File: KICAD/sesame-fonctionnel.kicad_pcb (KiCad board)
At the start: 2 copper layers, 160 x 100 mm, 278 parts, among them J1 CXS70-14-C, J2 CXS70-14-C, J7 CXS70-14-C, J8 CXS70-14-C, J9 Conn_02x16_Odd_Even, Q1 BC847, Q10 BC857, Q11 SQM120, Q12 BC847, Q13 BC847, Q2 BC847, Q3 BC847, Q4 BC847, Q5 BC847, Q6 SQM120, Q7 BC857, Q8 SQM120, Q9 SQM120, U1 AD8030, U10 LT6016, U11 AD8030, U12 UCC27284-Q1, U13 AD8030, U14 AD8030, U15 LT8365, U16 LM4040DBZ-2.5, U17 UCC27284-Q1, U2 LM2903, U3 CD4053BM96, U4 4011, U5 CD4053BM96, U6 CD4053BM96, U7 AD8030, U8 LT6016, U9 AD8030

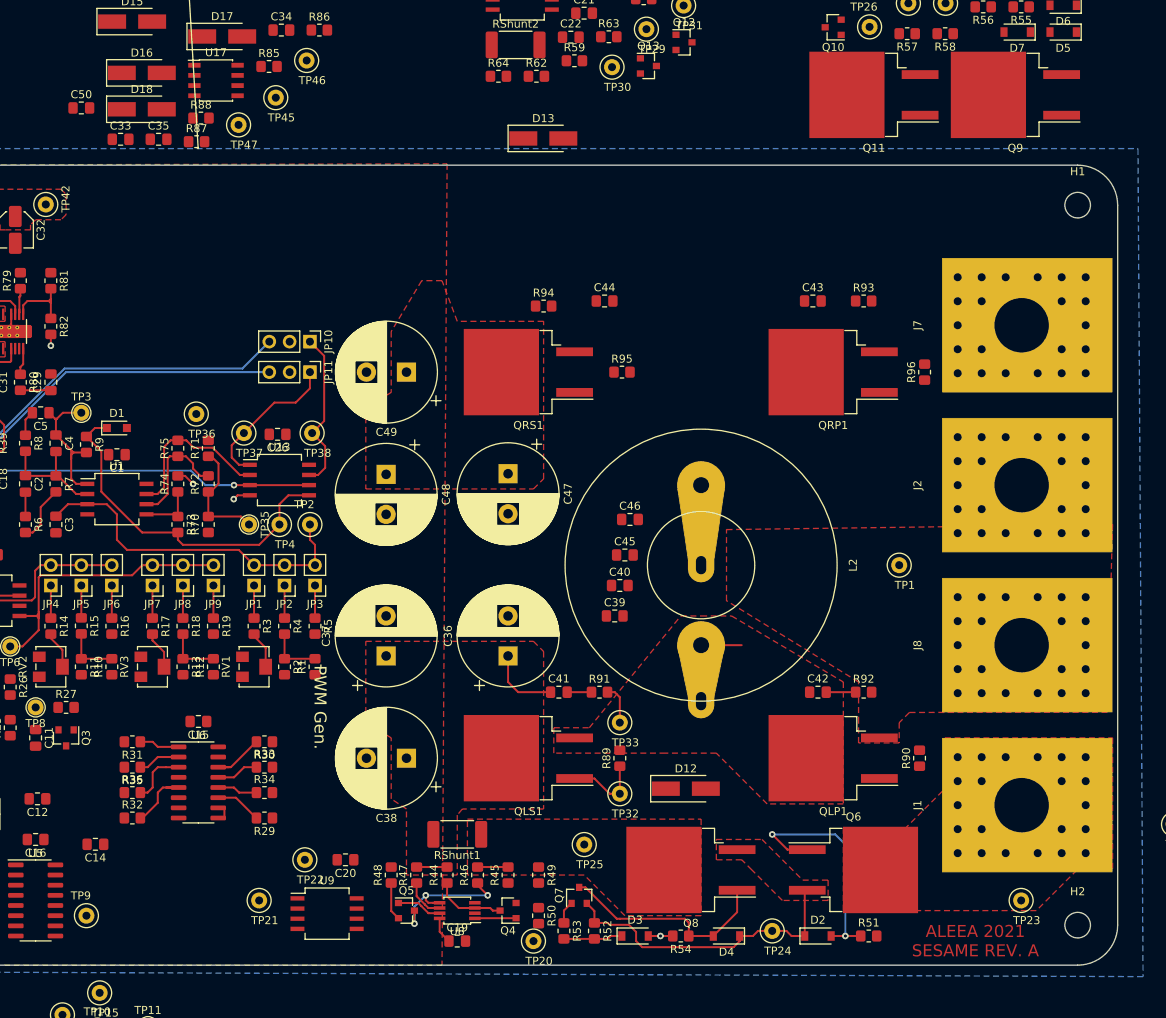
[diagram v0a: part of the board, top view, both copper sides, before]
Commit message: little cleanup. 278 conn. to go
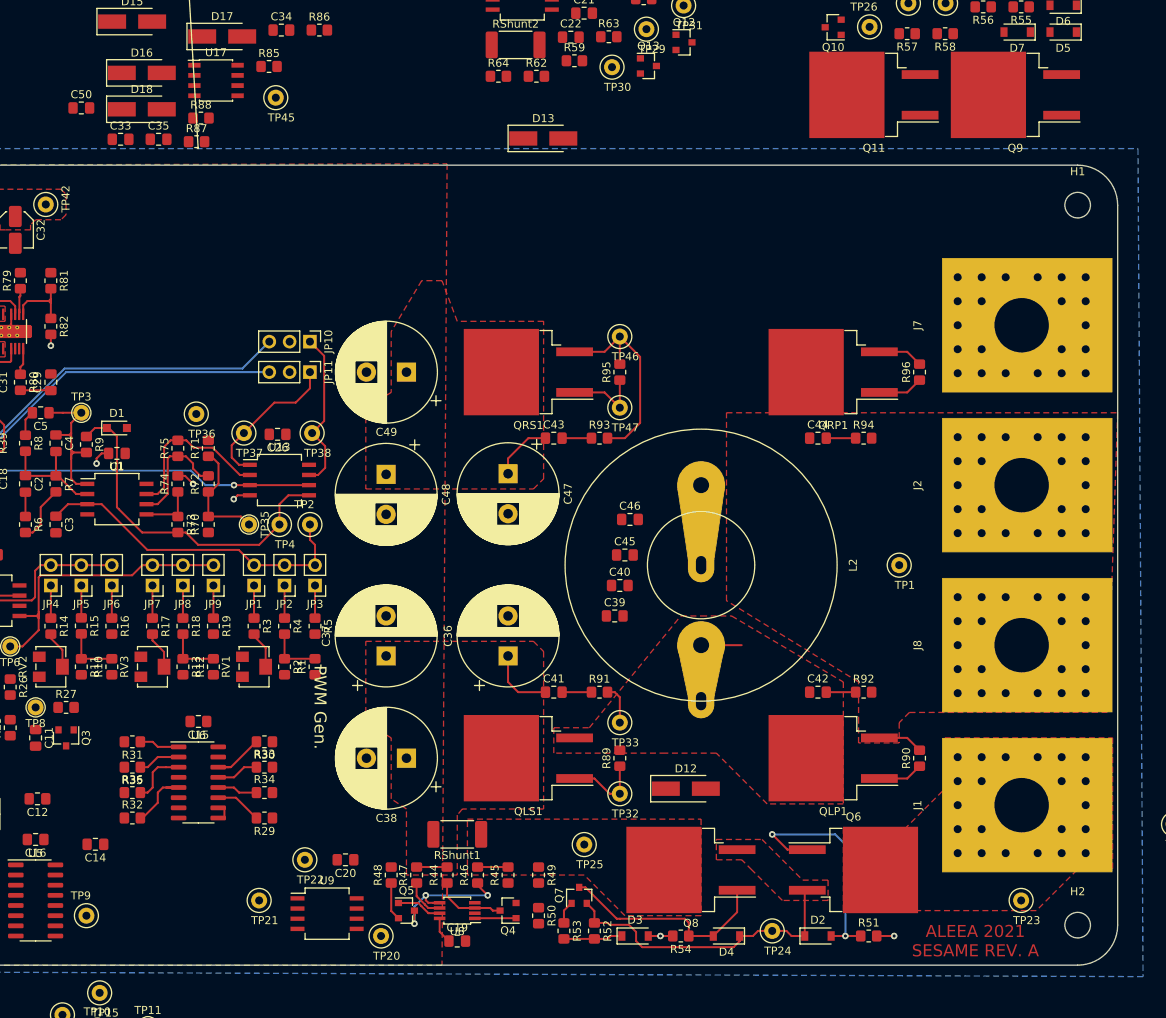
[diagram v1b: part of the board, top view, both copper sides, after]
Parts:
- moved TP47 59.3 mm to (177.8, 90.3)
- moved TP46 52.2 mm to (177.8, 81.4)
- moved R94 43.3 mm to (208.2, 94.1)
- moved R93 37.2 mm to (175.2, 94.1)
- moved C43 36.6 mm to (169.5, 94.1)
- moved C44 31.7 mm to (202.5, 94.1)
- moved TP20 19.1 mm to (147.9, 156.4)
- moved C41 0.64 mm to (169.5, 125.9)
- moved R96 0.63 mm to (215.2, 85.9)
- moved R95 0.27 mm to (177.8, 85.9), turned to 90 degrees
- moved C1 0.16 mm to (114.9, 96.0)
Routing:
- net /MOS DRIVER R/VS: track 0.00 -> 26.6 mm
- net GND: track 19.3 -> 35.2 mm, vias 10 -> 12
- net /MOS DRIVER R/VG_P: track 0.00 -> 9.89 mm
- net /U/I SENSOR RIGHT/VD_Mos: track 0.00 -> 7.63 mm
- net /DC/DC CONVERTER/VG_RP: track 0.00 -> 5.66 mm
- net /DC/DC CONVERTER/VG_LP: track 0.00 -> 5.66 mm
- net Net-(C44-Pad2): track 0.00 -> 3.68 mm
- net Net-(C43-Pad2): track 0.00 -> 3.68 mm
- net /PID/Feedback_raw: track 18.5 -> 20.5 mm
- net /PID/PID_Setpoint: track 43.4 -> 41.5 mm
- net /DC/DC CONVERTER/VD_LS: track 12.9 -> 12.3 mm
- net Net-(C41-Pad2): track 3.04 -> 3.68 mm
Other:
- board text added: "PID"

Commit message: clean up eco user 2 layer
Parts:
- moved C45 45.9 mm to (148.8, 73.7), turned to 180 degrees
- moved C40 44.1 mm to (148.2, 145.3), turned to 180 degrees
- moved C46 40.6 mm to (148.6, 77.5), turned to 180 degrees
- moved C39 39.2 mm to (148.0, 142.6), turned to 180 degrees
- moved U4 0.99 mm to (94.6, 153.2)
- moved C17 0.64 mm to (91.8, 92.2)
- moved C13 0.63 mm to (94.6, 146.2)
- moved U12 0.63 mm to (127.0, 189.4)
- turned C8 to 0 degrees
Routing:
- net VCC: track 3.32 -> 34.4 mm
- net GND: track 35.2 -> 51.2 mm, vias 12 -> 19
- net /Dir: track 0.00 -> 14.4 mm
- net Net-(C8-Pad1): track 10.1 -> 8.76 mm
- net Net-(R39-Pad1): track 20.8 -> 21.6 mm
- net /Mode: track 6.56 -> 5.93 mm
- net Net-(U4-Pad10): track 11.9 -> 12.4 mm
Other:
- board text added: "SEPIC supply"
- board text removed: "Feedback"
- board text removed: "Sepic sa mere"

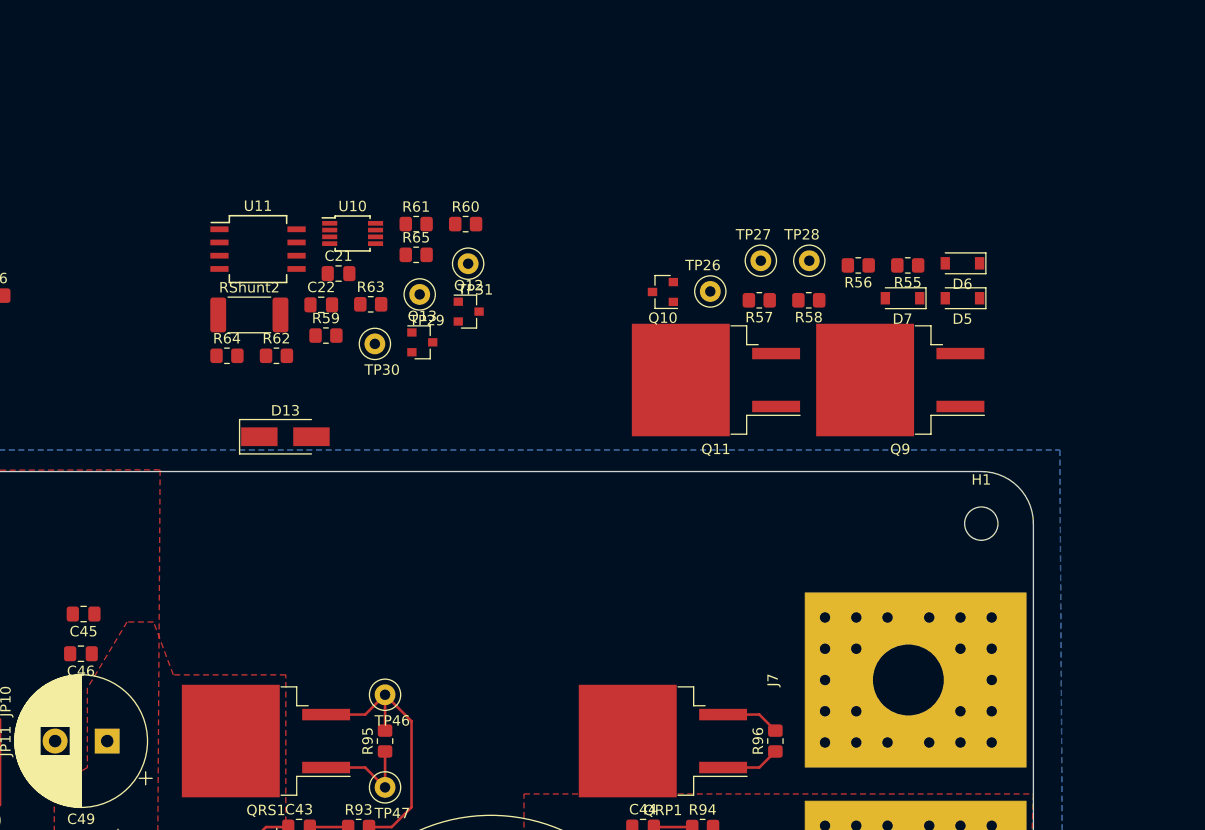
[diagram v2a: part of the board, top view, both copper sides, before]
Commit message: protect right. 249 conn.
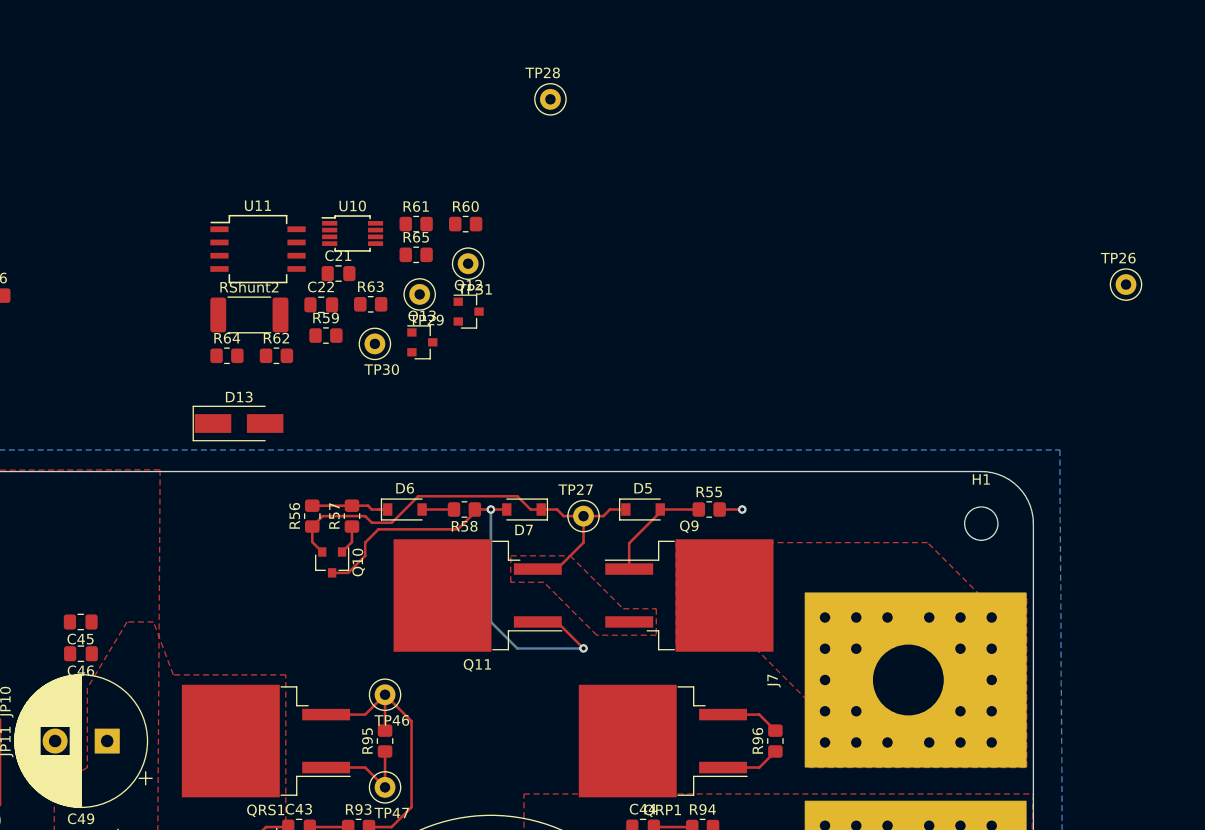
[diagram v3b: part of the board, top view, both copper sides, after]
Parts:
- moved D6 58.5 mm to (179.7, 63.6), turned to 0 degrees
- moved R56 57.7 mm to (170.8, 64.3), turned to 90 degrees
- moved R57 44.2 mm to (174.6, 64.3), turned to 90 degrees
- moved D7 41.6 mm to (191.1, 63.6)
- moved Q10 41.0 mm to (172.7, 68.7), turned to 270 degrees
- moved TP26 39.9 mm to (248.9, 42.1)
- moved R58 38.7 mm to (185.4, 63.6)
- moved D5 36.8 mm to (202.5, 63.6), turned to 0 degrees
- moved Q11 30.8 mm to (186.7, 71.9)
- moved R55 30.2 mm to (208.9, 63.6), turned to 0 degrees
- moved TP27 29.8 mm to (196.8, 64.3)
- moved TP28 29.3 mm to (193.6, 24.3)
- moved Q9 28.9 mm to (207.0, 71.9), turned to 0 degrees
- moved D13 4.62 mm to (163.8, 55.4)
- moved C45 0.81 mm to (148.6, 74.4)
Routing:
- net Net-(D7-Pad2): track 0.00 -> 46.4 mm, vias 0 -> 2
- net Net-(D5-Pad1): track 0.00 -> 43.7 mm
- net Net-(D5-Pad2): track 0.00 -> 10.6 mm
- net Net-(D6-Pad1): track 0.00 -> 7.39 mm
- net GND: track 51.2 -> 56.5 mm, vias 19 -> 20
- net Net-(Q10-Pad1): track 0.00 -> 3.11 mm
- added copper zone on F.Cu, net Net-(D5-Pad1)
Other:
- board text added: "PROTECT Left"
- board text added: "PROTECT Right"
- board text removed: "Protect"
- board text removed: "copie protect"

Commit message: 200 conn. remaining
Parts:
- moved TP28 153.1 mm to (168.9, 175.4)
- moved R60 141.1 mm to (158.7, 174.8), turned to 270 degrees
- moved R61 139.7 mm to (162.5, 174.8), turned to 270 degrees
- moved TP30 136.5 mm to (144.8, 180.5)
- moved U11 135.8 mm to (144.8, 172.9), turned to 90 degrees
- moved RShunt2 134.4 mm to (157.4, 179.2), turned to 180 degrees
- moved U10 133.7 mm to (157.4, 169.7)
- moved R63 133.1 mm to (150.5, 174.5), turned to 270 degrees
- moved C22 132.9 mm to (139.0, 172.9), turned to 270 degrees
- moved TP31 132.1 mm to (143.5, 165.2)
- moved Q12 130.5 mm to (150.5, 170.3)
- moved R59 129.3 mm to (152.4, 174.8), turned to 270 degrees
- moved R65 127.4 mm to (177.1, 166.5), turned to 90 degrees
- moved R62 126.4 mm to (155.5, 174.8), turned to 270 degrees
- moved TP29 126.0 mm to (168.9, 168.4)
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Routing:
- net /DC/DC CONVERTER/VG_LP: track 5.66 -> 104.4 mm, vias 0 -> 2
- net /MOS DRIVER L/VS: track 10.0 -> 92.9 mm, vias 0 -> 2
- net /Ext_Setpoint: track 0.00 -> 57.5 mm, vias 0 -> 1
- net /Current_Thres: track 0.00 -> 55.5 mm, vias 0 -> 1
- net /DC/DC CONVERTER/VG_LS: track 9.89 -> 60.2 mm, vias 0 -> 2
- net Net-(R49-Pad2): track 0.00 -> 43.8 mm
- net GND: track 56.5 -> 87.0 mm, vias 20 -> 53
- net Net-(Q4-Pad2): track 4.77 -> 33.2 mm
- net Net-(D9-Pad1): track 0.00 -> 27.9 mm
- net Net-(D8-Pad1): track 0.00 -> 25.5 mm
- net /Voltage_Thres: track 0.00 -> 15.7 mm, vias 0 -> 1
- net VCC: track 34.4 -> 46.9 mm
- net Net-(C24-Pad1): track 0.00 -> 11.0 mm
- net /Voltage_Sens_L: track 0.00 -> 10.6 mm
- net Net-(R45-Pad1): track 0.00 -> 8.77 mm
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- added copper zone on F.Cu, net /MOS DRIVER R/VS
- added copper zone on F.Cu, net /R
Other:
- board text added: "Driver Left"
- board text added: "U/I SENS Left"
- board text removed: "Power supply"
- board text removed: "Ref"

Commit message: ui sens right. 170 conn.
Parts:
- moved R63 111.5 mm to (152.4, 63.0), turned to 0 degrees
- moved TP29 106.4 mm to (147.3, 64.3)
- moved R60 103.5 mm to (160.0, 71.3)
- moved R61 103.5 mm to (163.8, 71.3)
- moved R62 103.5 mm to (156.2, 71.3)
- moved Q12 103.5 mm to (151.1, 66.8)
- moved R59 103.5 mm to (152.4, 71.3)
- moved RShunt2 102.9 mm to (157.4, 76.3)
- moved U10 102.9 mm to (157.4, 66.8)
- moved Q13 102.2 mm to (163.8, 66.8)
- moved C21 102.2 mm to (157.4, 63.0)
- moved TP30 101.0 mm to (140.9, 79.5)
- moved TP31 101.0 mm to (140.9, 64.3)
- moved R64 100.8 mm to (167.6, 71.3)
- moved R65 100.8 mm to (167.6, 66.2)
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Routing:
- net Net-(Q12-Pad2): track 0.00 -> 37.1 mm
- net Net-(R64-Pad2): track 0.00 -> 36.0 mm
- net /INT EXT CONFIG/Ext_PWM: track 81.7 -> 54.7 mm
- net /INT EXT CONFIG/~Ext_PWM: track 75.6 -> 50.2 mm
- net /INT_PWM_Power: track 20.2 -> 9.54 mm
- net /Voltage_Sens_R: track 0.00 -> 10.3 mm
- net GND: track 87.0 -> 96.8 mm, vias 53 -> 57
- net /Current_Sens_R: track 0.00 -> 9.22 mm
- net Net-(R60-Pad1): track 0.00 -> 8.75 mm, vias 0 -> 2
- net VCC: track 46.9 -> 55.2 mm
- net /U/I SENSOR RIGHT/VD_Mos: track 7.63 -> 15.2 mm
- net Net-(Q13-Pad3): track 0.00 -> 7.41 mm
- net Net-(Q13-Pad1): track 0.00 -> 7.14 mm
- net Net-(Q12-Pad3): track 0.00 -> 6.84 mm
- net Net-(R62-Pad1): track 0.00 -> 5.66 mm
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- added copper zone on F.Cu, net /VProt_Right
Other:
- board text added: "Driver Right"
- board text added: "I/O Conn."
- board text added: "U/I SENS Right"
- board text removed: "copie ui sens"
- board text removed: "driver"

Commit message: right driver done. 149 conn.
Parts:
- moved TP12 86.0 mm to (70.5, 186.8)
- moved TP15 64.0 mm to (89.5, 183.7)
- moved TP16 46.2 mm to (89.5, 193.8)
- moved TP14 44.2 mm to (89.5, 179.8)
- moved TP10 37.8 mm to (78.7, 184.9)
- moved TP13 36.9 mm to (85.1, 195.1)
- moved C34 35.4 mm to (114.9, 71.9)
- moved TP11 31.0 mm to (78.7, 188.1)
- moved R86 29.9 mm to (130.1, 71.3), turned to 180 degrees
- moved TP17 28.4 mm to (89.5, 197.6)
- moved D16 27.0 mm to (122.5, 75.1), turned to 180 degrees
- moved D18 26.5 mm to (132.7, 75.1)
- moved D17 24.0 mm to (132.7, 67.5)
- moved D15 22.3 mm to (122.5, 63.6)
- moved TP9 22.2 mm to (100.9, 134.1)
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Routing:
- net /DC/DC CONVERTER/VG_RP: track 9.25 -> 108.1 mm, vias 0 -> 2
- net /MOS DRIVER R/VS: track 26.6 -> 108.4 mm, vias 0 -> 2
- net /MOS DRIVER R/VG_P: track 9.89 -> 71.9 mm, vias 0 -> 2
- net Net-(D15-Pad1): track 0.00 -> 27.0 mm
- net Net-(D16-Pad1): track 0.00 -> 21.0 mm
- net GND: track 96.8 -> 117.4 mm, vias 57 -> 59
- net Net-(C34-Pad1): track 0.00 -> 11.0 mm
- net VCC: track 55.2 -> 62.8 mm
- net /U/I SENSOR RIGHT/VD_Mos: track 15.2 -> 8.00 mm
- net Net-(D18-Pad1): track 0.00 -> 4.21 mm
- net Net-(D17-Pad1): track 0.00 -> 4.21 mm
- net Net-(D8-Pad1): track 25.5 -> 27.7 mm

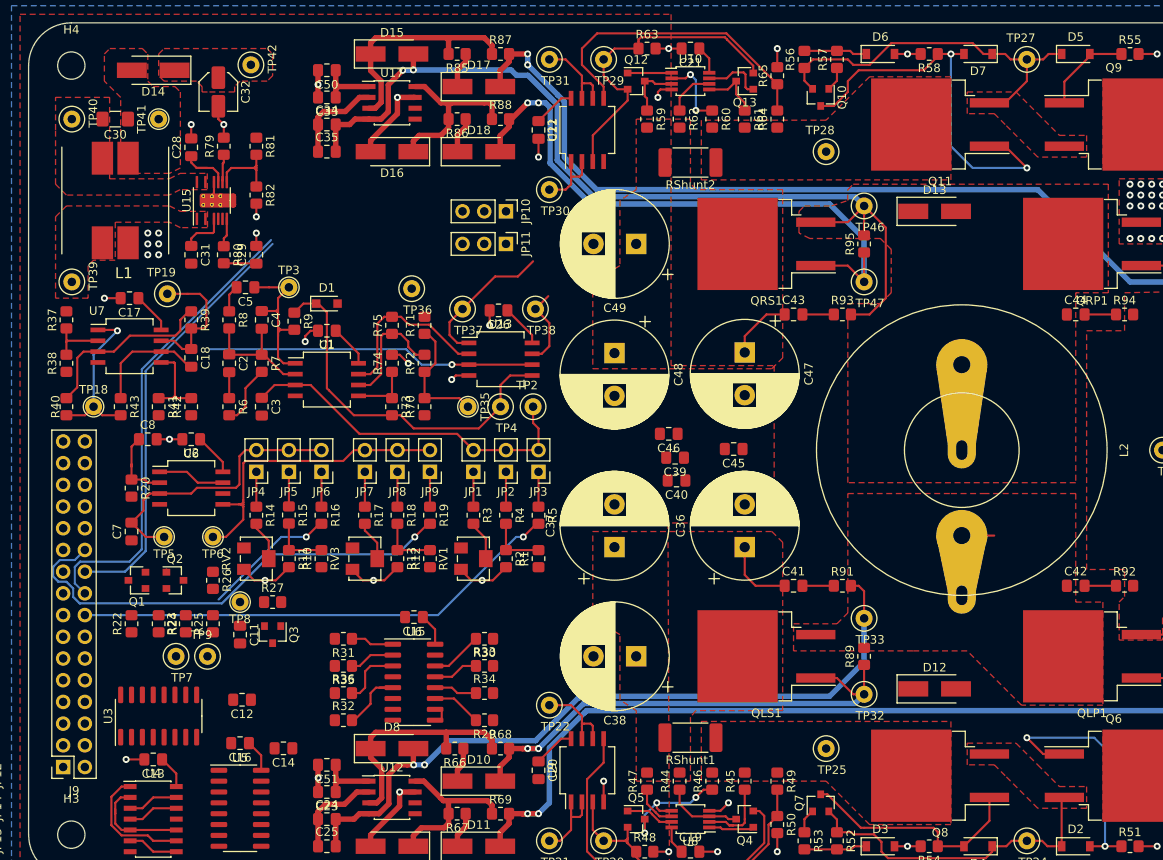
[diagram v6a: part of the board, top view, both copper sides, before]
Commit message: 144 conn. will convert to 4 layers
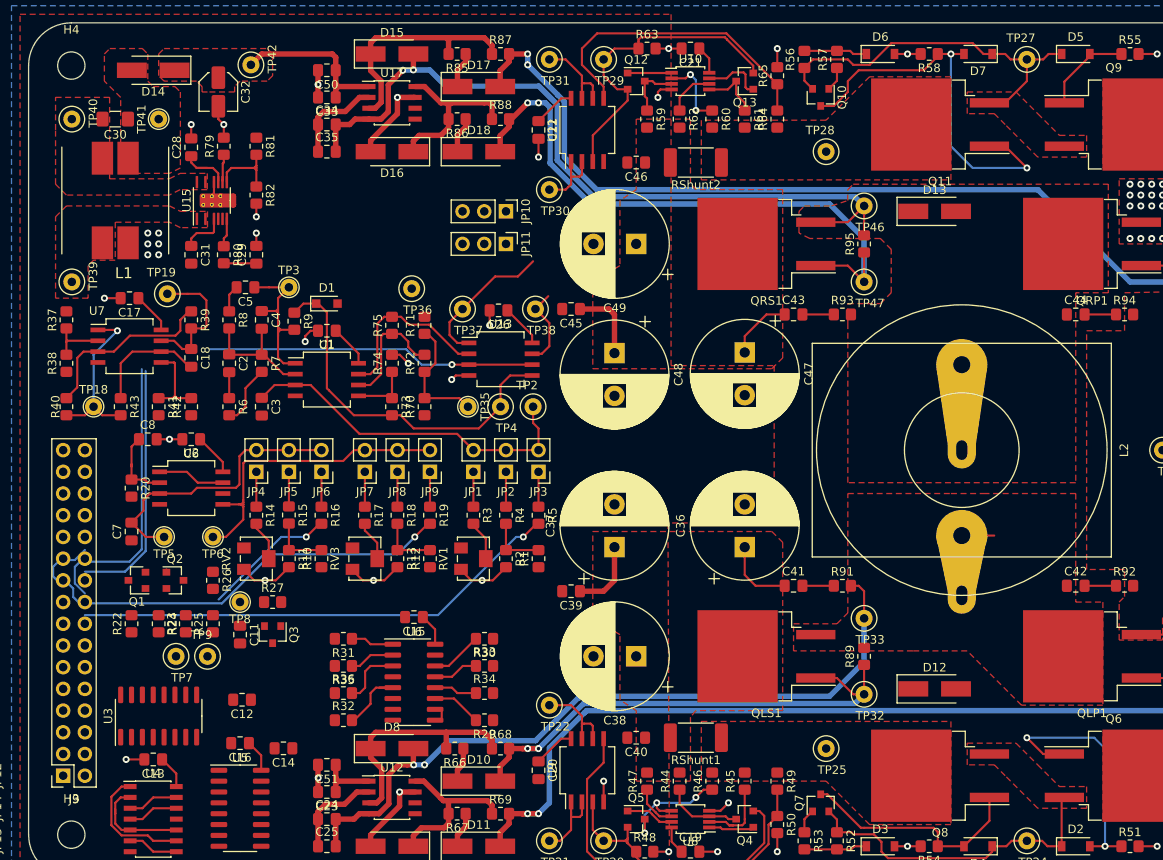
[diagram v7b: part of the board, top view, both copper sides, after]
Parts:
- moved C46 32.0 mm to (151.1, 76.3)
- moved C40 30.5 mm to (151.1, 143.7)
- moved C45 25.1 mm to (143.5, 93.5)
- moved C39 19.8 mm to (143.5, 126.5)
- moved J9 1.02 mm to (84.0, 148.1)
- moved RShunt1 0.64 mm to (158.1, 143.7)
- moved RShunt2 0.64 mm to (158.1, 76.3)
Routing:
- net /INT EXT CONFIG/Ext_PWM: track 54.7 -> 0.00 mm
- net /Current_Thres: track 55.5 -> 88.9 mm
- net /INT EXT CONFIG/~Ext_PWM: track 50.2 -> 29.2 mm
- net /MOS DRIVER R/VS: track 108.4 -> 91.7 mm
- net VCC: track 62.8 -> 74.9 mm
- net /U/I SENSOR RIGHT/VD_Mos: track 8.00 -> 16.8 mm
- net /DC/DC CONVERTER/VD_LS: track 8.46 -> 16.9 mm
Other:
- board text added: "outline en mm placement des composants en 1.27mm 160x100"
- board text removed: "outline en mm placement des composants en 1.27 160x100"

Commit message: test w/ layers indicator
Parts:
- added REF**: Layer_indicator_2L, Sesame_footprint:Layer_indicator, F.Cu at (222.9, 63.6)
- moved C26 0.28 mm to (135.2, 93.5)
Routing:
- net /Current_Thres: track 88.9 -> 28.2 mm
- net /Ext_Setpoint: track 57.5 -> 16.2 mm
- net /INT EXT CONFIG/~Ext_PWM: track 29.2 -> 0.00 mm
- net VCC: track 74.9 -> 90.4 mm, vias 0 -> 12
- net /PWM GEN/Ramp: track 54.6 -> 65.0 mm
- net GND: track 117.4 -> 125.1 mm, vias 59 -> 60
- net /~INT_PWM_Freewheel: track 16.9 -> 11.7 mm
- net /INT_PWM_Power: track 9.54 -> 7.41 mm
- net Net-(R39-Pad1): track 21.6 -> 23.1 mm
- added copper zone on F.Cu, net (none)
- added copper zone on In1.Cu, net VCC
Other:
- copper layers 2 -> 4
